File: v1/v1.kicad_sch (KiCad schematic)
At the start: 0 parts

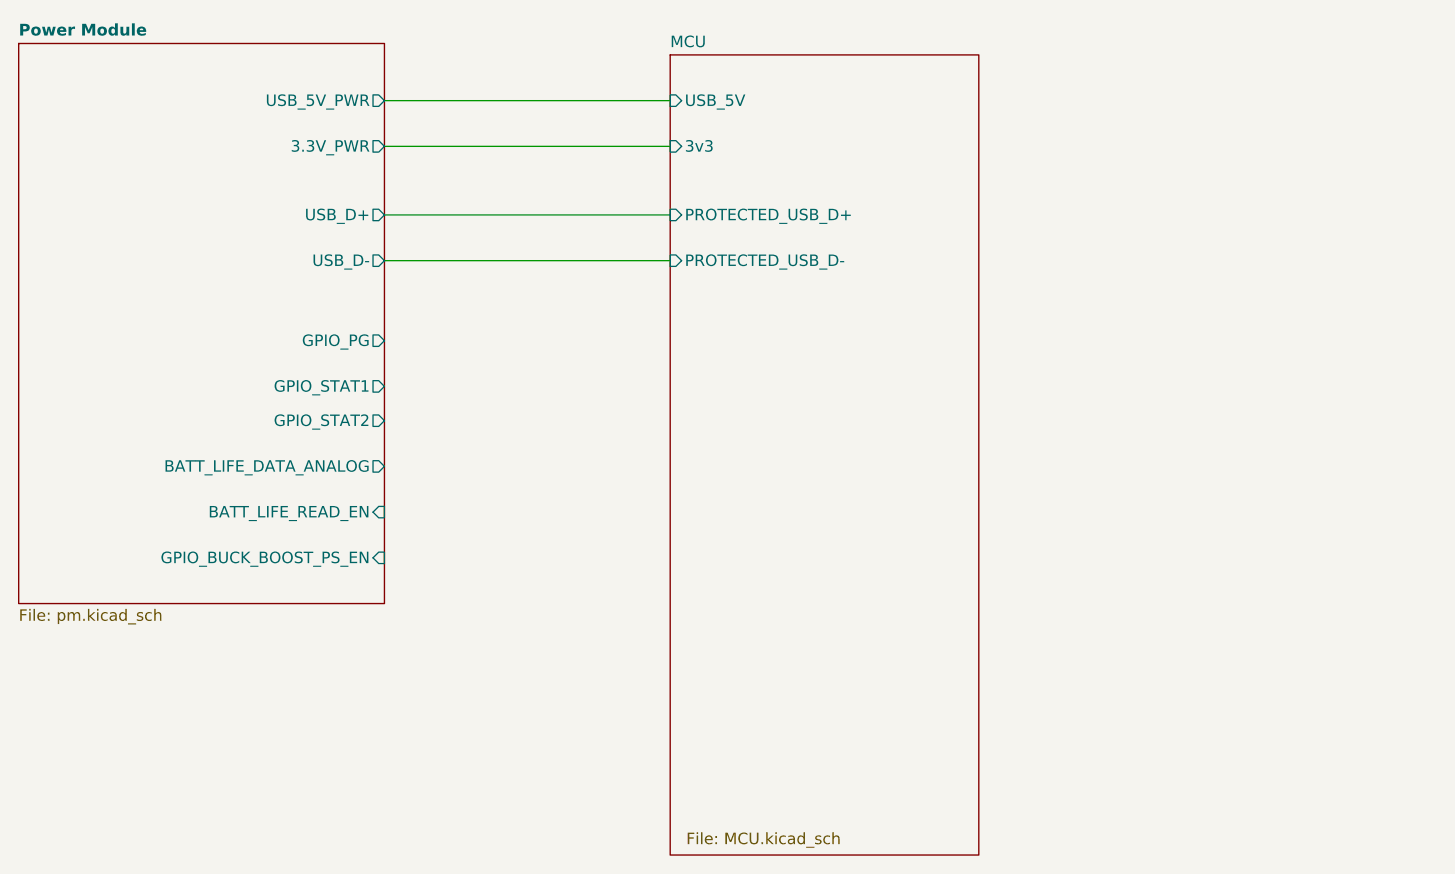
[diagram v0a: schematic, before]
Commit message: Updated layout
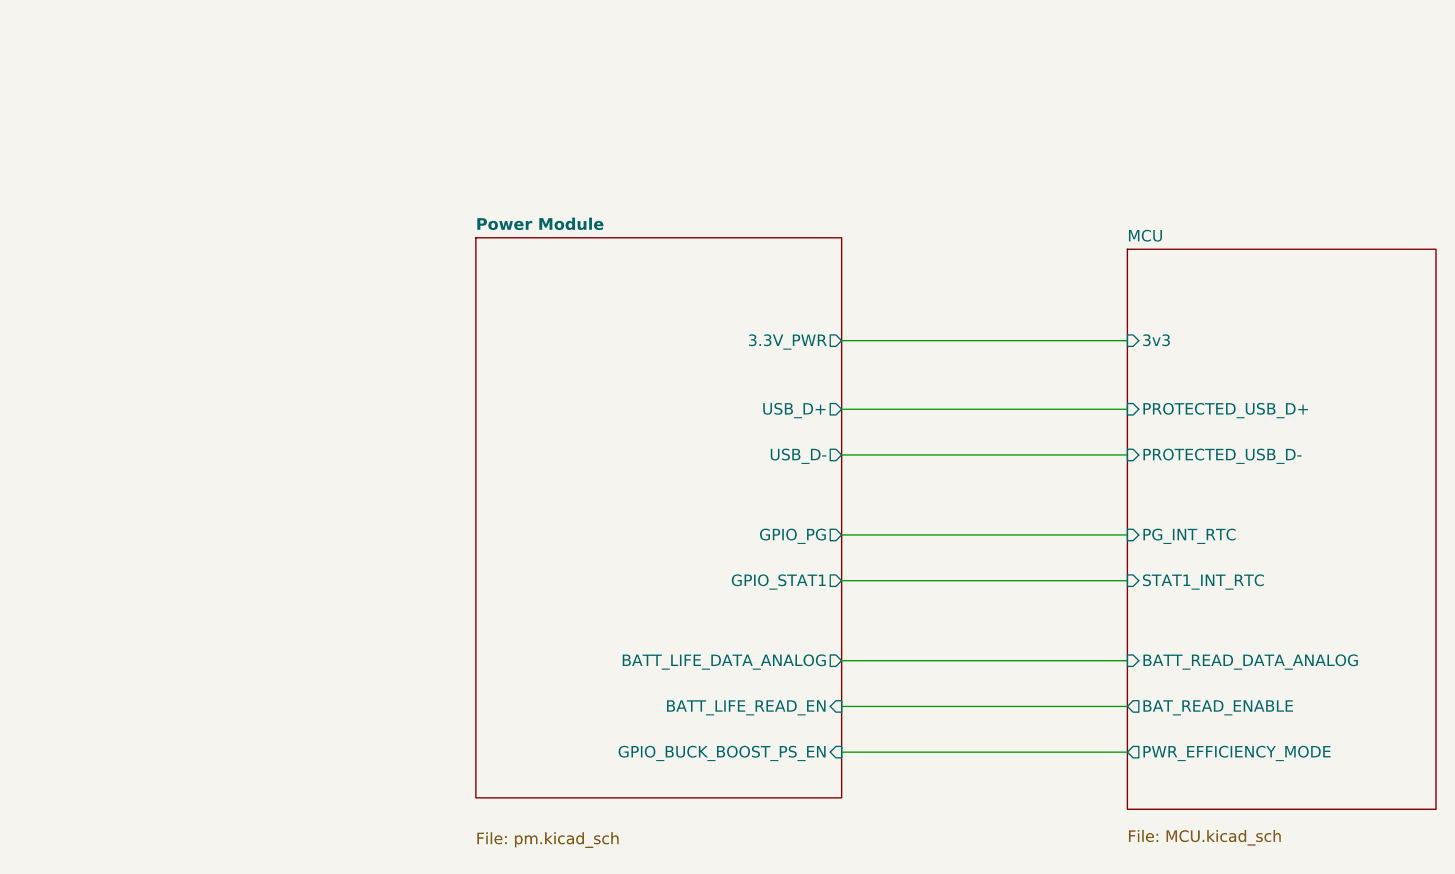
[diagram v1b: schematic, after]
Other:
- sheet MCU ports: added BATT_READ_DATA_ANALOG, BAT_READ_ENABLE, PG_INT_RTC, PWR_EFFICIENCY_MODE, STAT1_INT_RTC; removed USB_5V
- sheet Power Module ports: added none; removed GPIO_STAT2, USB_5V_PWR
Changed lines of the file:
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@@
 	(wire
 		(pts
-			(xy 74.93 54.61) (xy 106.68 54.61)
-		)
-		(stroke
-			(width 0)
-			(type default)
-		)
-	)
-	(wire
-		(pts
-			(xy 74.93 41.91) (xy 106.68 41.91)
-		)
-		(stroke
-			(width 0)
-			(type default)
-		)
-	)
-	(wire
-		(pts
-			(xy 74.93 46.99) (xy 106.68 46.99)
-		)
-		(stroke
-			(width 0)
-			(type default)
-		)
-	)
-	(wire
-		(pts
-			(xy 74.93 59.69) (xy 106.68 59.69)
+			(xy 125.73 114.3) (xy 157.48 114.3)
+		)
+		(stroke
+			(width 0)
+			(type default)
+		)
+	)
+	(wire
+		(pts
+			(xy 125.73 109.22) (xy 157.48 109.22)
+		)
+		(stroke
+			(width 0)
+			(type default)
+		)
+	)
+	(wire
+		(pts
+			(xy 125.73 104.14) (xy 157.48 104.14)
+		)
+		(stroke
+			(width 0)
+			(type default)
+		)
+	)
+	(wire
+		(pts
+			(xy 125.73 90.17) (xy 157.48 90.17)
+		)
+		(stroke
+			(width 0)
+			(type default)
+		)
+	)
+	(wire
+		(pts
+			(xy 125.73 76.2) (xy 157.48 76.2)
+		)
+		(stroke
+			(width 0)
+			(type default)
+		)
+	)
+	(wire
+		(pts
+			(xy 125.73 95.25) (xy 157.48 95.25)
+		)
+		(stroke
+			(width 0)
+			(type default)
+		)
+	)
+	(wire
+		(pts
+			(xy 125.73 68.58) (xy 157.48 68.58)
+		)
+		(stroke
+			(width 0)
+			(type default)
+		)
+	)
+	(wire
+		(pts
+			(xy 125.73 81.28) (xy 157.48 81.28)
 		)
 		(stroke
@@
 	)
 	(sheet
-		(at 34.29 35.56)
+		(at 85.09 57.15)
 		(size 40.64 62.23)
 		(exclude_from_sim no)
@@
 		(on_board yes)
 		(dnp no)
-		(fields_autoplaced yes)
 		(stroke
 			(width 0.1524)
@@
 		)
 		(property "Sheetname" "Power Module"
-			(at 34.29 34.8334 0)
+			(at 85.09 56.4234 0)
 			(effects
 				(font
@@
 		)
 		(property "Sheetfile" "pm.kicad_sch"
-			(at 34.29 98.3746 0)
+			(at 85.09 123.19 0)
 			(effects
 				(font
@@
 		)
 		(pin "3.3V_PWR" output
-			(at 74.93 46.99 0)
+			(at 125.73 68.58 0)
 			(effects
 				(font
@@
 		)
 		(pin "USB_D+" output
-			(at 74.93 54.61 0)
+			(at 125.73 76.2 0)
 			(effects
 				(font
@@
 		)
 		(pin "USB_D-" output
-			(at 74.93 59.69 0)
+			(at 125.73 81.28 0)
 			(effects
 				(font
@@
 		)
 		(pin "GPIO_PG" output
-			(at 74.93 68.58 0)
+			(at 125.73 90.17 0)
 			(effects
 				(font
@@
 		)
 		(pin "GPIO_STAT1" output
-			(at 74.93 73.66 0)
-			(effects
-				(font
-					(size 1.27 1.27)
-				)
-				(justify right)
-			)
-		)
-		(pin "GPIO_STAT2" output
-			(at 74.93 77.47 0)
+			(at 125.73 95.25 0)
 			(effects
 				(font
@@
 		)
 		(pin "BATT_LIFE_DATA_ANALOG" output
-			(at 74.93 82.55 0)
+			(at 125.73 104.14 0)
 			(effects
 				(font
@@
 		)
 		(pin "BATT_LIFE_READ_EN" input
-			(at 74.93 87.63 0)
+			(at 125.73 109.22 0)
 			(effects
 				(font
@@
 		)
 		(pin "GPIO_BUCK_BOOST_PS_EN" input
-			(at 74.93 92.71 0)
-			(effects
-				(font
-					(size 1.27 1.27)
-				)
-				(justify right)
-			)
-		)
-		(pin "USB_5V_PWR" output
-			(at 74.93 41.91 0)
+			(at 125.73 114.3 0)
 			(effects
 				(font
@@
 	)
 	(sheet
-		(at 106.68 36.83)
-		(size 34.29 88.9)
+		(at 157.48 58.42)
+		(size 34.29 62.23)
 		(exclude_from_sim no)
 		(in_bom yes)
@@
 		)
 		(property "Sheetname" "MCU"
-			(at 106.68 36.1184 0)
+			(at 157.48 57.7084 0)
 			(effects
 				(font
@@
 		)
 		(property "Sheetfile" "MCU.kicad_sch"
-			(at 108.458 123.19 0)
+			(at 157.48 122.936 0)
 			(effects
 				(font
@@
 		)
 		(pin "3v3" input
-			(at 106.68 46.99 180)
+			(at 157.48 68.58 180)
 			(effects
 				(font
@@
 		)
 		(pin "PROTECTED_USB_D+" input
-			(at 106.68 54.61 180)
+			(at 157.48 76.2 180)
 			(effects
 				(font
@@
 		)
 		(pin "PROTECTED_USB_D-" input
-			(at 106.68 59.69 180)
-			(effects
-				(font
-					(size 1.27 1.27)
-				)
-				(justify left)
-			)
-		)
-		(pin "USB_5V" input
-			(at 106.68 41.91 180)
-			(effects
-				(font
+			(at 157.48 81.28 180)
+			(effects
+				(font
+					(size 1.27 1.27)
+				)
+				(justify left)
+			)
+		)
+		(pin "BAT_READ_ENABLE" output
+			(at 157.48 109.22 180)
+			(effects
+				(font
+					(size 1.27 1.27)
+				)
+				(justify left)
+			)
+		)
+		(pin "PWR_EFFICIENCY_MODE" output
+			(at 157.48 114.3 180)
+			(effects
+				(font
+					(size 1.27 1.27)
+				)
+				(justify left)
+			)
+		)
+		(pin "BATT_READ_DATA_ANALOG" input
+			(at 157.48 104.14 180)
+			(effects
+				(font
+					(size 1.27 1.27)
+				)
+				(justify left)
+			)
+		)
+		(pin "PG_INT_RTC" input
+			(at 157.48 90.17 180)
+			(effects
+				(font
+					(size 1.27 1.27)
+				)
+				(justify left)
+			)
+		)
+		(pin "STAT1_INT_RTC" input
+			(at 157.48 95.25 180)
+			(effects
+				(font
